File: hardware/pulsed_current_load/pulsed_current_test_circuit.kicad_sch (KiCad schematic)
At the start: 17 parts, among them J1 Conn_02x03_Odd_Even, J2 Conn_02x03_Odd_Even, U1 eALD1116SAL, U2 eALD1116SAL, U3 eALD1116SAL

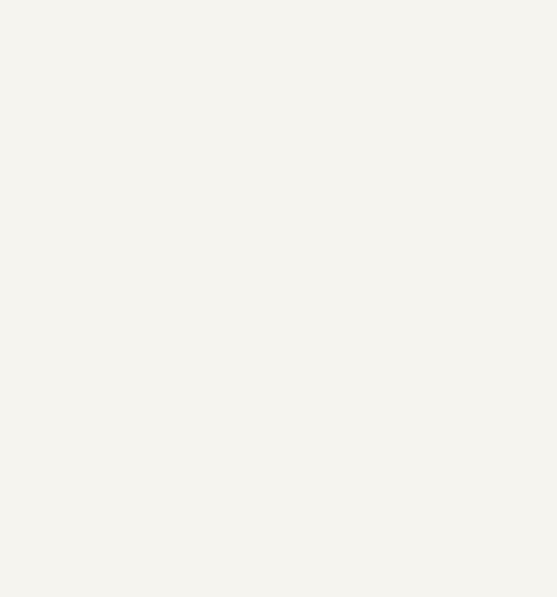
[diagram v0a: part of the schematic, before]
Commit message: added test pads to fixture boards
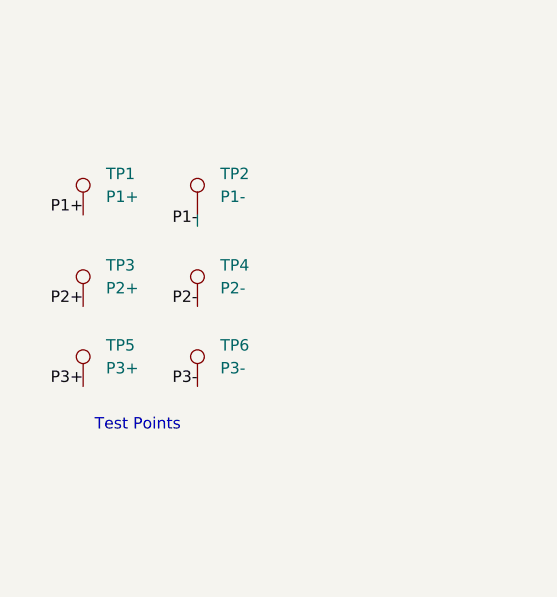
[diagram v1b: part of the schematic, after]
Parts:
- added TP1: P1+, TestPoint:TestPoint_Pad_1.5x1.5mm, symbol Connector:TestPoint
- added TP2: P1-, TestPoint:TestPoint_Pad_1.5x1.5mm, symbol Connector:TestPoint
- added TP3: P2+, TestPoint:TestPoint_Pad_1.5x1.5mm, symbol Connector:TestPoint
- added TP4: P2-, TestPoint:TestPoint_Pad_1.5x1.5mm, symbol Connector:TestPoint
- added TP5: P3+, TestPoint:TestPoint_Pad_1.5x1.5mm, symbol Connector:TestPoint
- added TP6: P3-, TestPoint:TestPoint_Pad_1.5x1.5mm, symbol Connector:TestPoint
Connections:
- net GND: now also TP2.1, TP4.1, TP6.1
- net P1+: now also TP1.1
- net P2+: now also TP3.1
- net P3+: now also TP5.1
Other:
- note added: "Test Points"
